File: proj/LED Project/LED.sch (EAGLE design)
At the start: 19 parts, among them J3 AVR_SPI_PROG_3X2NS, U2 ATMEGA328P_MLF, Y1 16MHz

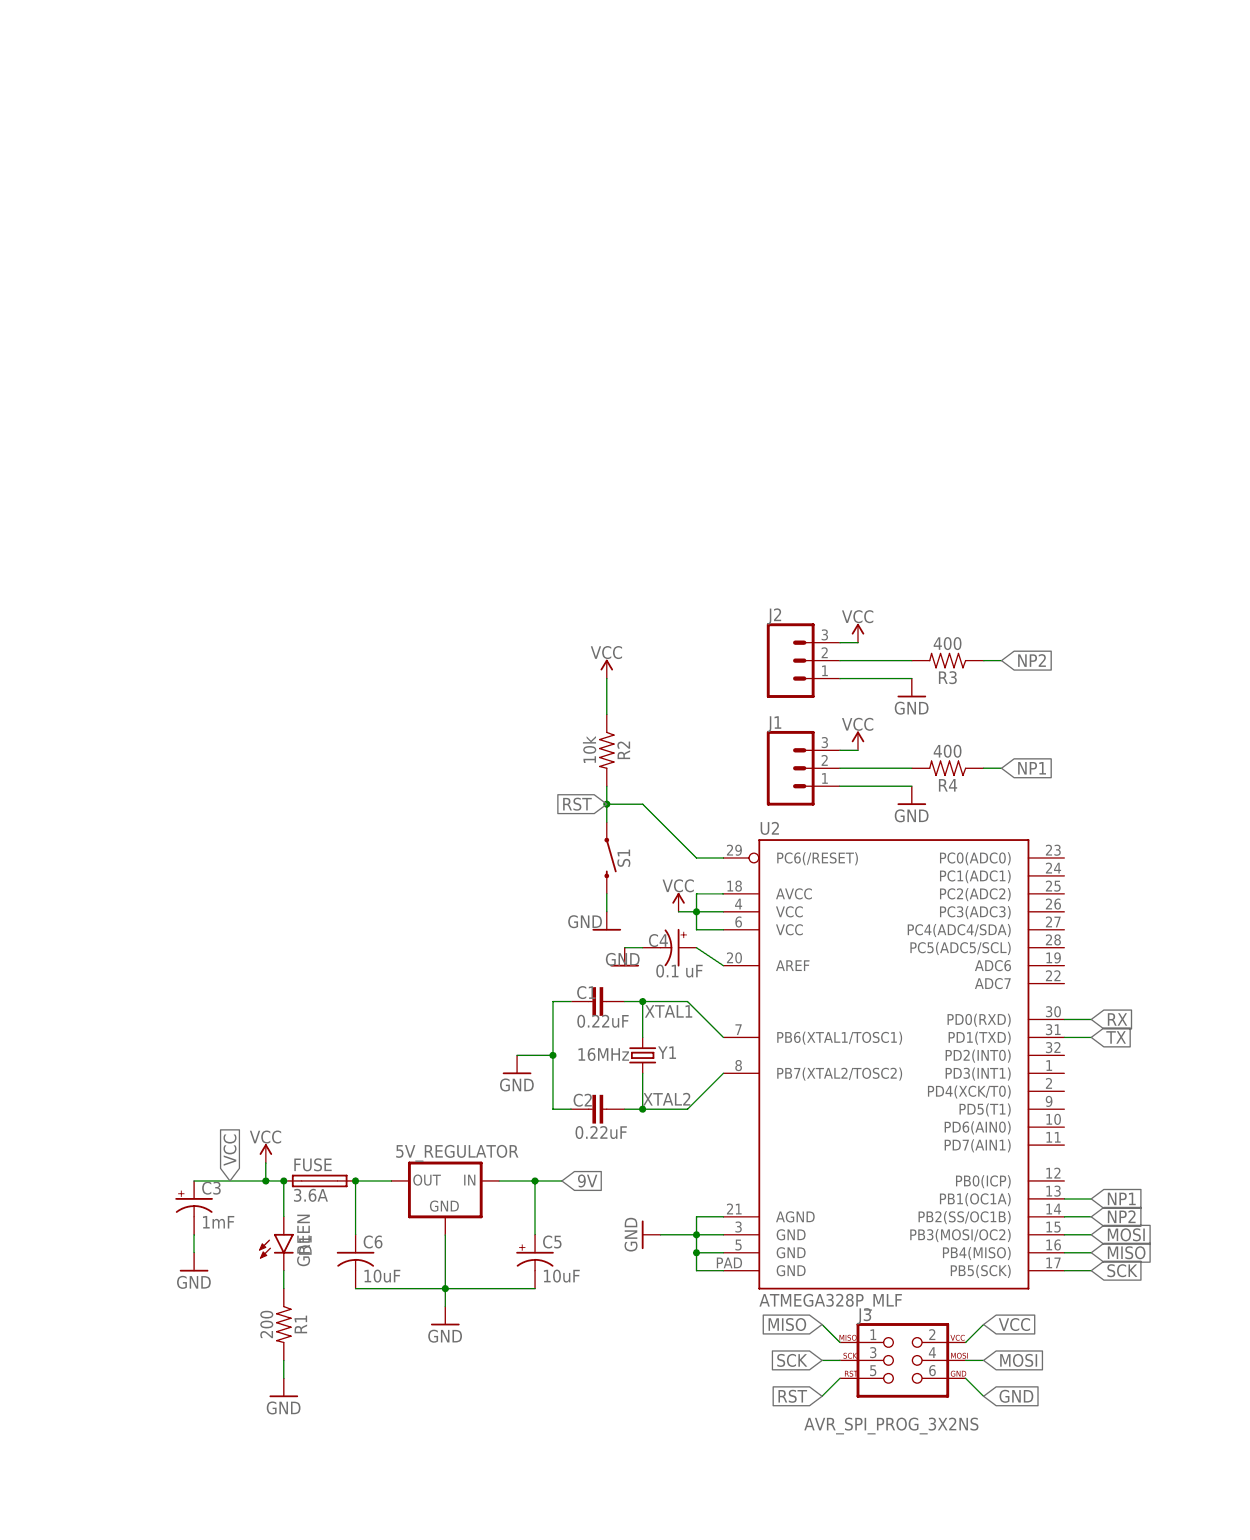
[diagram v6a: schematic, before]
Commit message: Reorganzing the Schematic and adding documentation
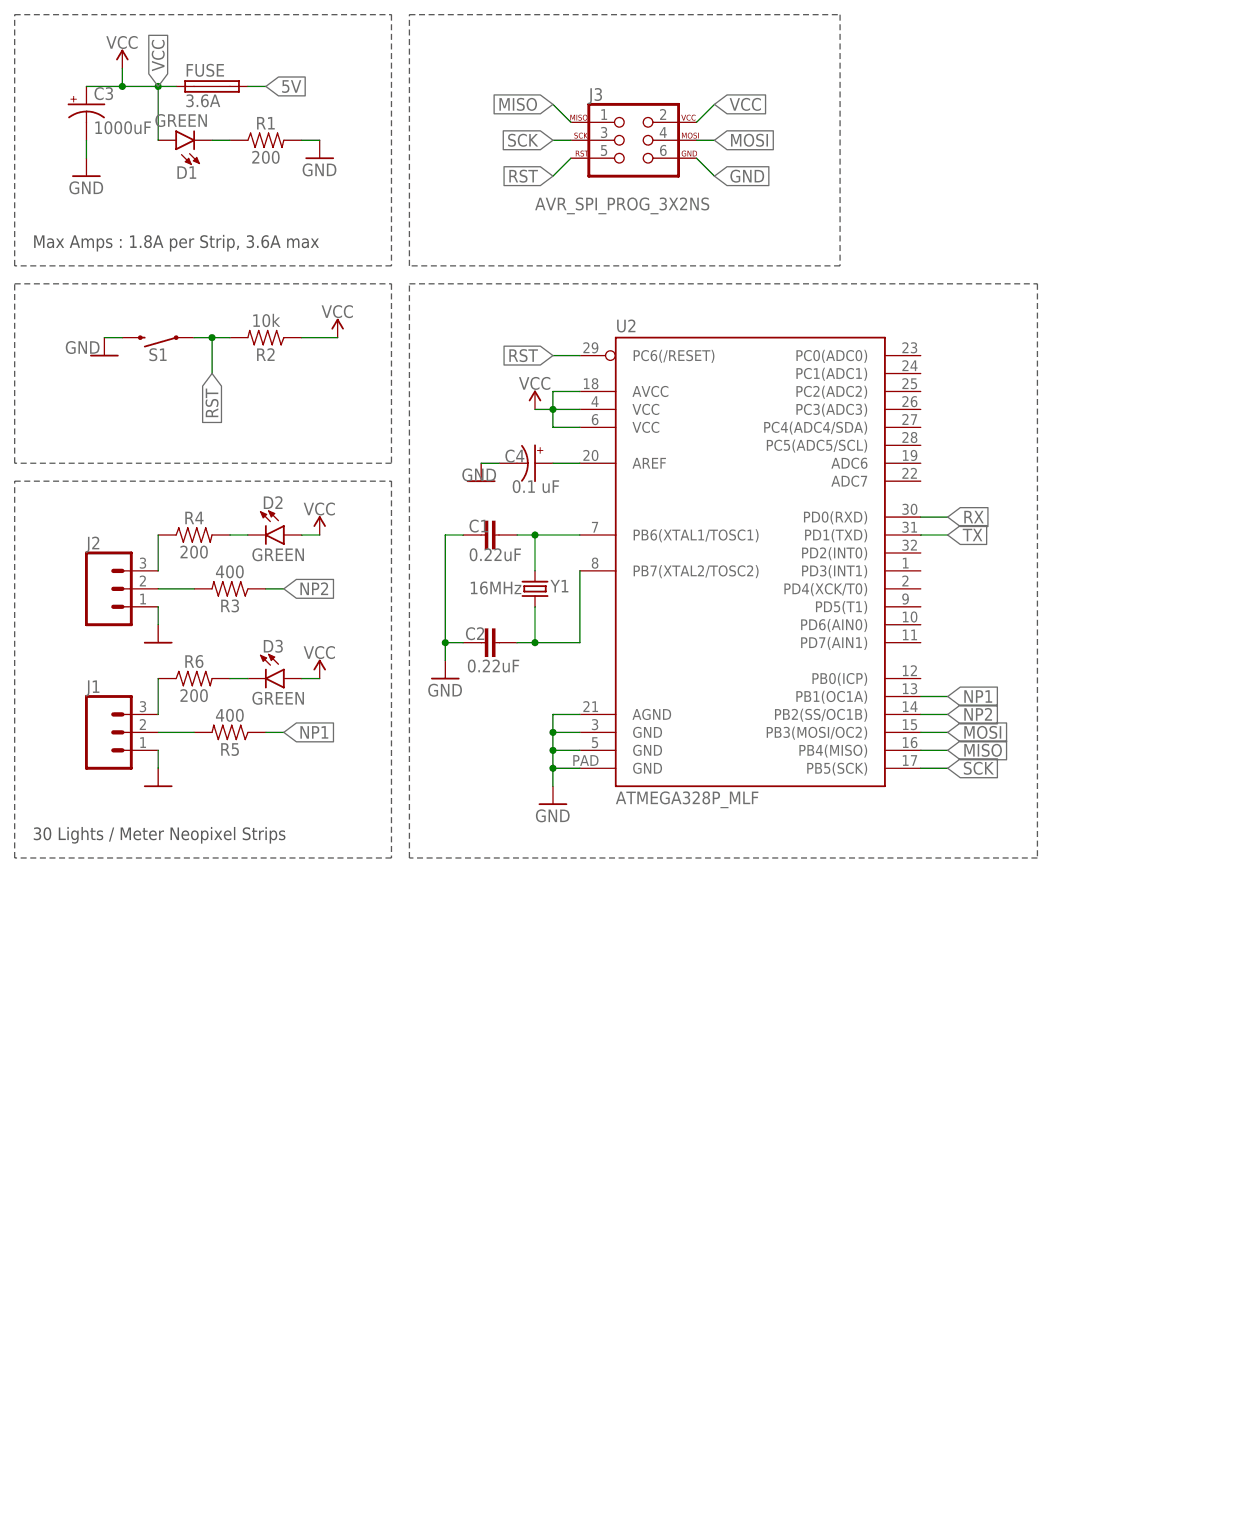
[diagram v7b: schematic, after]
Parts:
- removed 5V_REGULATOR: R-78E5.0-1.0, SparkFun-IC-Power:R-78E5.0-1.0
- removed C5: 10uF, SparkFun-Capacitors:1000UF-RADIAL-5MM-25V-20%
- removed C6: 10uF, rcl:C-USC0805
- added D2, D3: GREEN, SparkFun-LED:LED-GREEN0603
- added R5: 400, SparkFun-Resistors:470OHM-0603-1/10W-1%
- added R6: 200, SparkFun-Resistors:470OHM-0603-1/10W-1%
- C3: value 1mF -> 1000uF
- J1: SPICEPREFIX (none) -> J
- R4: value 400 -> 200
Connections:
- removed net 9V: 5V_REGULATOR.IN, C5.+
- new net 5V: FUSE.2
- new net N$2: D2.C, R4.2
- new net N$3: J2.3, R4.1
- new net N$4: D3.C, R6.2
- net DATA1: now also R5.2; no longer R4.2
- net GND: no longer 5V_REGULATOR.GND, C5.-, C6.2
- net N$5: now also J1.3, R6.1; no longer 5V_REGULATOR.OUT, C6.1, FUSE.2
- net NP1: now also R5.1; no longer R4.1
- net VCC: now also D2.A, D3.A; no longer J1.3, J2.3
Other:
- note added: "30 Lights / Meter Neopixel Strips"
- note added: "Max Amps : 1.8A per Strip, 3.6A max"
- moved on the sheet: C1, C2, C3, C4, D1, FUSE, J1, J2, J3, R1, R2, R3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

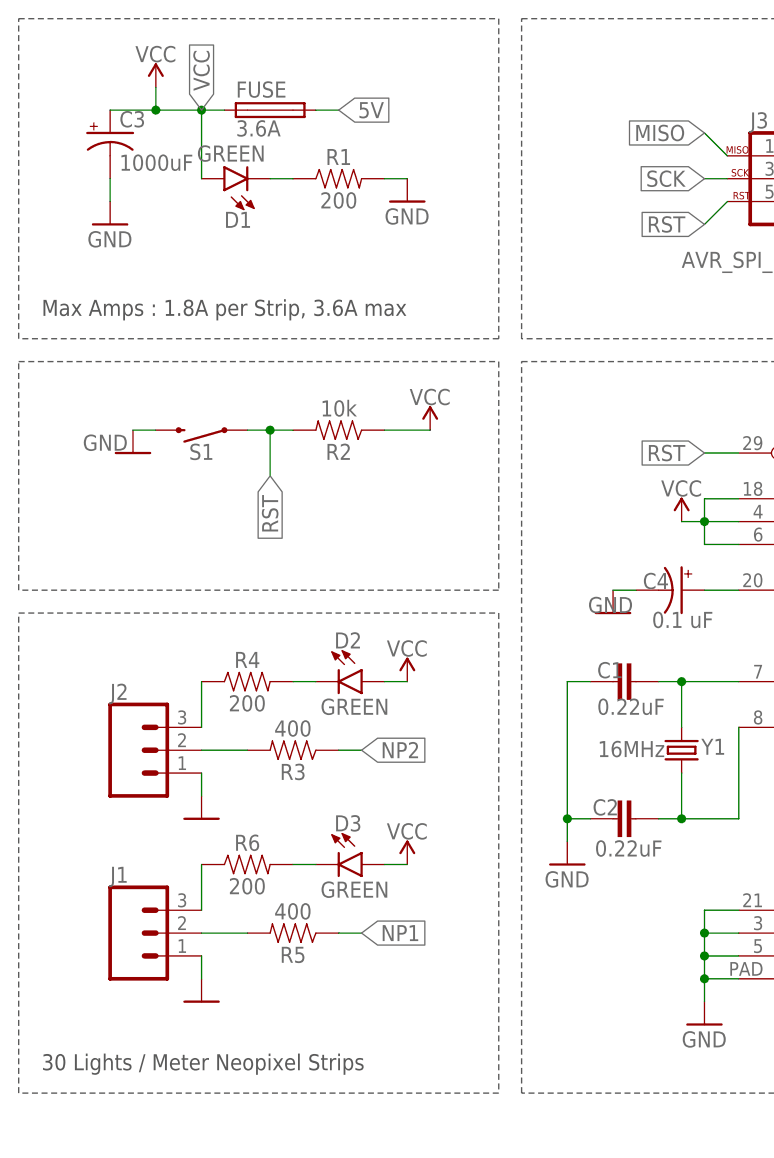
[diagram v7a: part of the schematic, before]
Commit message: Documentation + style changes
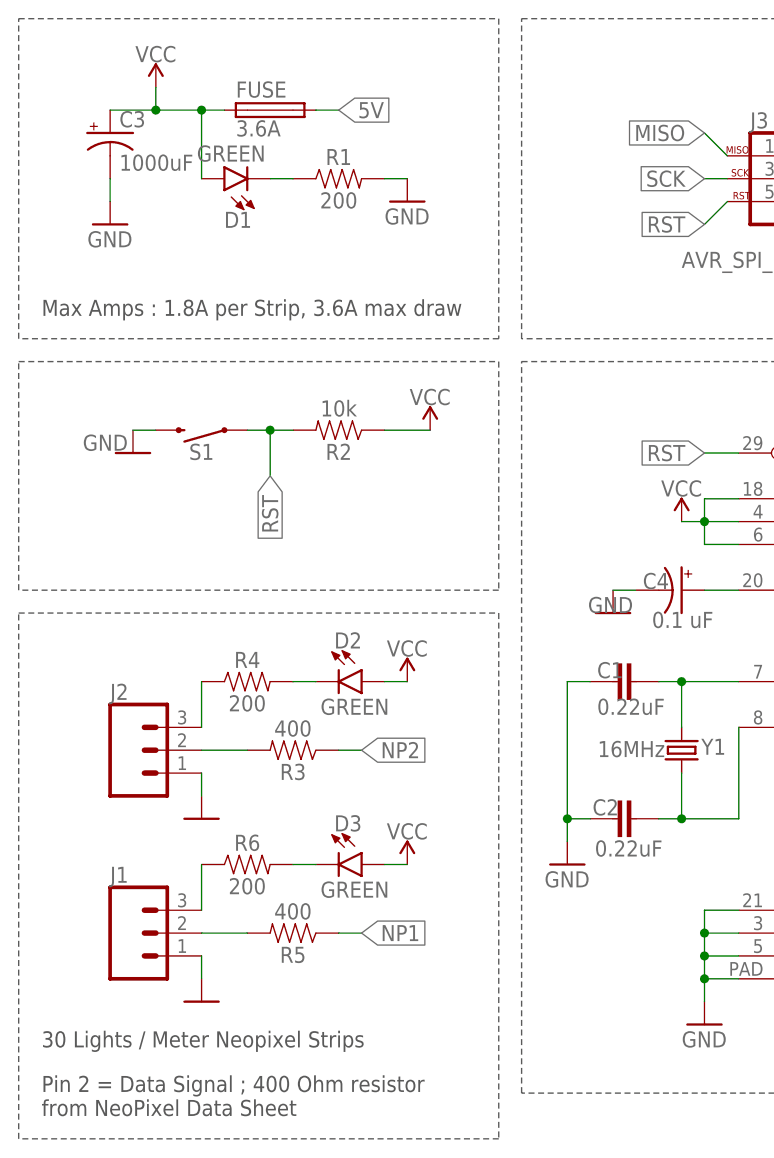
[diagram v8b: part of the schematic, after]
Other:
- note added: "Max Amps : 1.8A per Strip, 3.6A max draw"
- note added: "Pin 2 = Data Signal ; 400 Ohm resistor from NeoPixel Data Sheet"
- note removed: "Max Amps : 1.8A per Strip, 3.6A max"
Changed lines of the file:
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@@
 <?xml version="1.0" encoding="utf-8"?>
 <!DOCTYPE eagle SYSTEM "eagle.dtd">
-<eagle version="9.1.3">
+<eagle version="9.2.2">
 <drawing>
 <settings>
@@
 <wire x1="-45.72" y1="137.16" x2="-45.72" y2="162.56" width="0.1524" layer="97" style="shortdash"/>
 <wire x1="-45.72" y1="134.62" x2="7.62" y2="134.62" width="0.1524" layer="97" style="shortdash"/>
-<wire x1="7.62" y1="134.62" x2="7.62" y2="81.28" width="0.1524" layer="97" style="shortdash"/>
-<wire x1="7.62" y1="81.28" x2="-45.72" y2="81.28" width="0.1524" layer="97" style="shortdash"/>
-<wire x1="-45.72" y1="81.28" x2="-45.72" y2="134.62" width="0.1524" layer="97" style="shortdash"/>
+<wire x1="7.62" y1="134.62" x2="7.62" y2="76.2" width="0.1524" layer="97" style="shortdash"/>
+<wire x1="7.62" y1="76.2" x2="-45.72" y2="76.2" width="0.1524" layer="97" style="shortdash"/>
+<wire x1="-45.72" y1="76.2" x2="-45.72" y2="134.62" width="0.1524" layer="97" style="shortdash"/>
 <wire x1="10.16" y1="200.66" x2="71.12" y2="200.66" width="0.1524" layer="97" style="shortdash"/>
 <wire x1="71.12" y1="200.66" x2="71.12" y2="165.1" width="0.1524" layer="97" style="shortdash"/>
@@
 <wire x1="99.06" y1="81.28" x2="10.16" y2="81.28" width="0.1524" layer="97" style="shortdash"/>
 <wire x1="10.16" y1="81.28" x2="10.16" y2="162.56" width="0.1524" layer="97" style="shortdash"/>
-<text x="-43.18" y="167.64" size="1.778" layer="97">Max Amps : 1.8A per Strip, 3.6A max</text>
-<text x="-43.18" y="83.82" size="1.778" layer="97">30 Lights / Meter Neopixel Strips</text>
+<text x="-43.18" y="167.64" size="1.778" layer="97">Max Amps : 1.8A per Strip, 3.6A max draw</text>
+<text x="-43.18" y="86.36" size="1.778" layer="97">30 Lights / Meter Neopixel Strips</text>
+<text x="-43.18" y="78.74" size="1.778" layer="97">Pin 2 = Data Signal ; 400 Ohm resistor
+from NeoPixel Data Sheet</text>
 </plain>
 <instances>
@@
 <attribute name="VALUE" x="-21.59" y="187.579" size="1.778" layer="96"/>
 </instance>
-<instance part="FRAME1" gate="G$1" x="-50.8" y="-10.16"/>
-<instance part="FRAME1" gate="G$2" x="121.92" y="-10.16"/>
+<instance part="FRAME1" gate="G$1" x="-50.8" y="-10.16" smashed="yes"/>
+<instance part="FRAME1" gate="G$2" x="121.92" y="-10.16" smashed="yes">
+<attribute name="LAST_DATE_TIME" x="134.62" y="-8.89" size="2.54" layer="94" font="vector"/>
+<attribute name="SHEET" x="208.28" y="-8.89" size="2.54" layer="94" font="vector"/>
+<attribute name="DRAWING_NAME" x="137.16" y="8.89" size="2.54" layer="94" font="vector"/>
+</instance>
 <instance part="D2" gate="G$1" x="-7.62" y="127" smashed="yes" rot="R270">
 <attribute name="NAME" x="-10.668" y="130.683" size="1.778" layer="95" font="vector"/>
@@
 <wire x1="-30.48" y1="190.5" x2="-35.56" y2="190.5" width="0.1524" layer="91"/>
 <pinref part="C3" gate="G$1" pin="+"/>
+<pinref part="SUPPLY5" gate="G$1" pin="VCC"/>
 <wire x1="-22.86" y1="190.5" x2="-25.4" y2="190.5" width="0.1524" layer="91"/>
-<pinref part="SUPPLY5" gate="G$1" pin="VCC"/>
 <wire x1="-25.4" y1="190.5" x2="-30.48" y2="190.5" width="0.1524" layer="91"/>
 <wire x1="-30.48" y1="190.5" x2="-30.48" y2="193.04" width="0.1524" layer="91"/>
 <pinref part="FUSE" gate="G$1" pin="1"/>
-<label x="-25.4" y="190.5" size="1.778" layer="95" rot="R90" xref="yes"/>
 <junction x="-30.48" y="190.5"/>
 <pinref part="D1" gate="G$1" pin="A"/>
@@
 </drawing>
 <compatibility>
+<note version="6.3" minversion="6.2.2" severity="warning">
+Since Version 6.2.2 text objects can contain more than one line,
+which will not be processed correctly with this version.
+</note>
 <note version="8.2" severity="warning">
 Since Version 8.2, EAGLE supports online libraries. The ids
